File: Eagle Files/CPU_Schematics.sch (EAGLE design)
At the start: 28 parts, among them IC1 74HC574N, IC10 74HC574N, IC11 74LS541N, IC12 CY62256LL-PC, IC13 74AS04N, IC14 74AS04N, IC15 74S283N, IC16 74S283N, IC19 74ALS04N, IC2 74LS541N, IC20 74LS541N, IC3 4514N, IC4 74LS04N, IC5 74HC574N, IC6 74LS541N, IC7 CY62256LL-PC, IC8 74S283N, IC9 74S283N

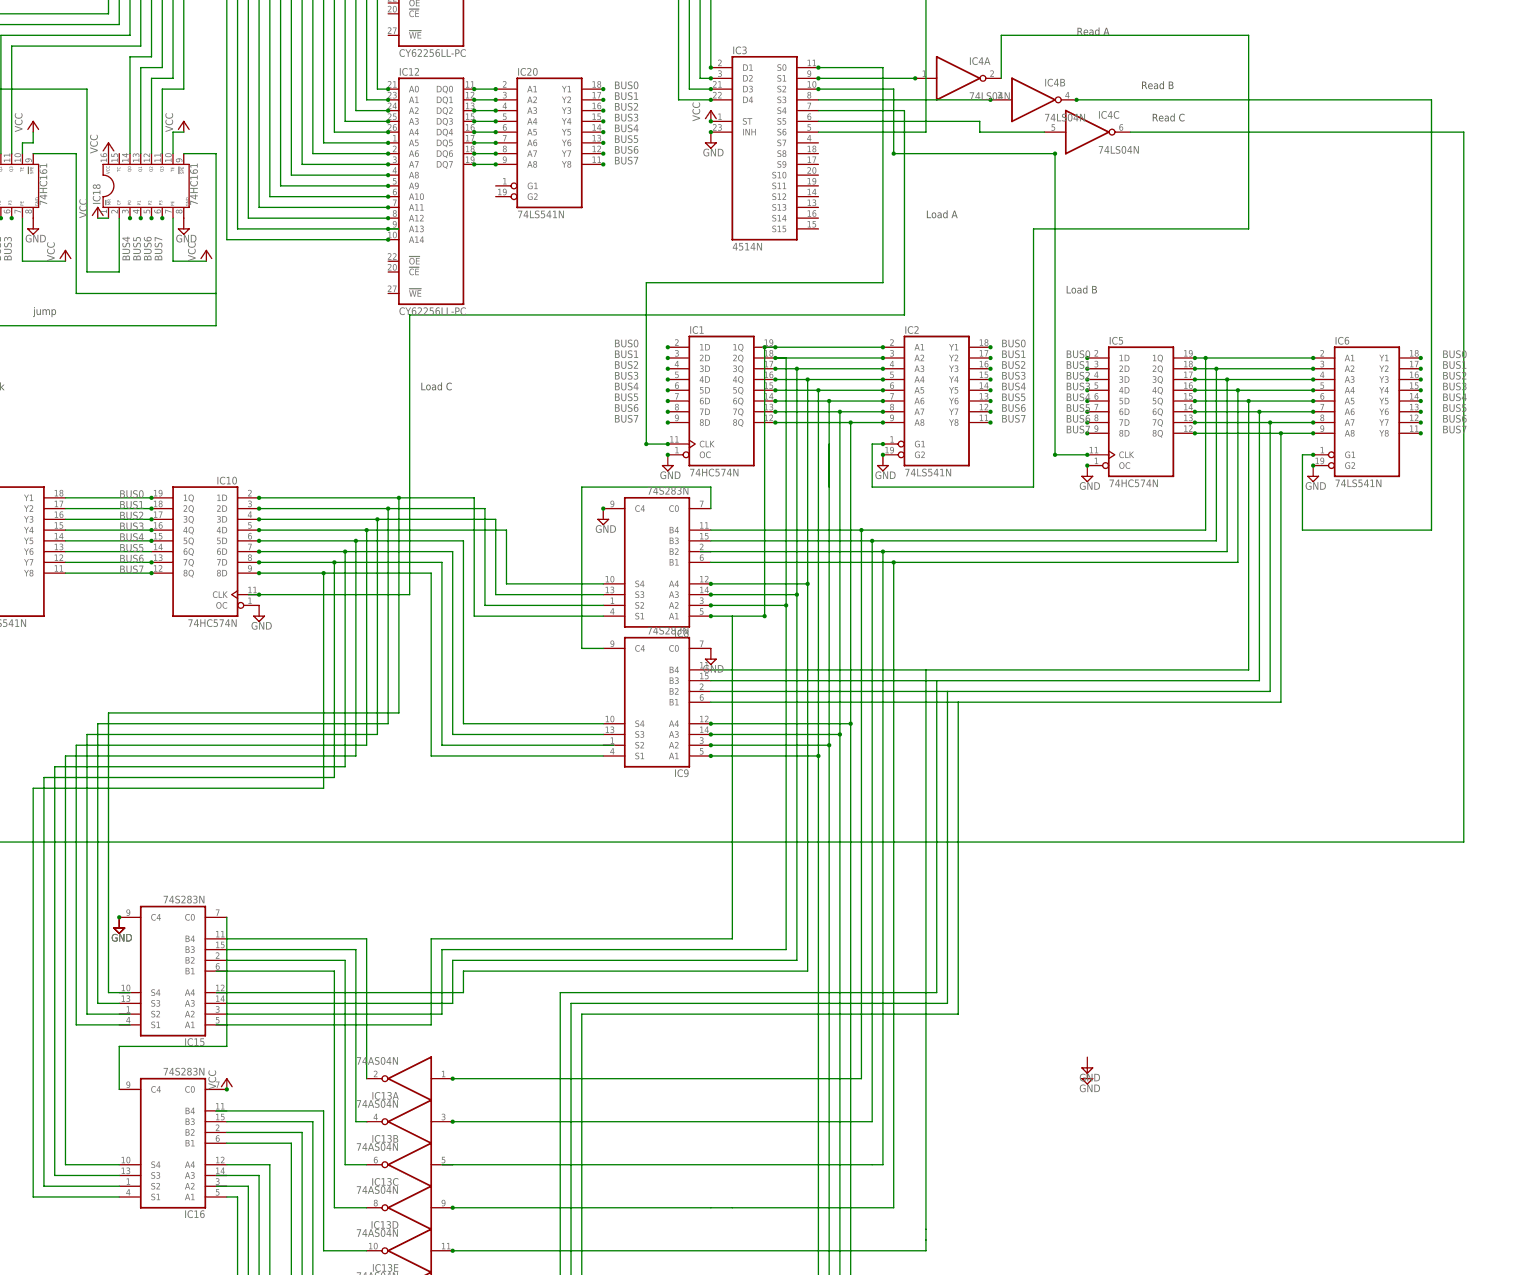
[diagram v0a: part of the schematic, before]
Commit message: Added RAM output control
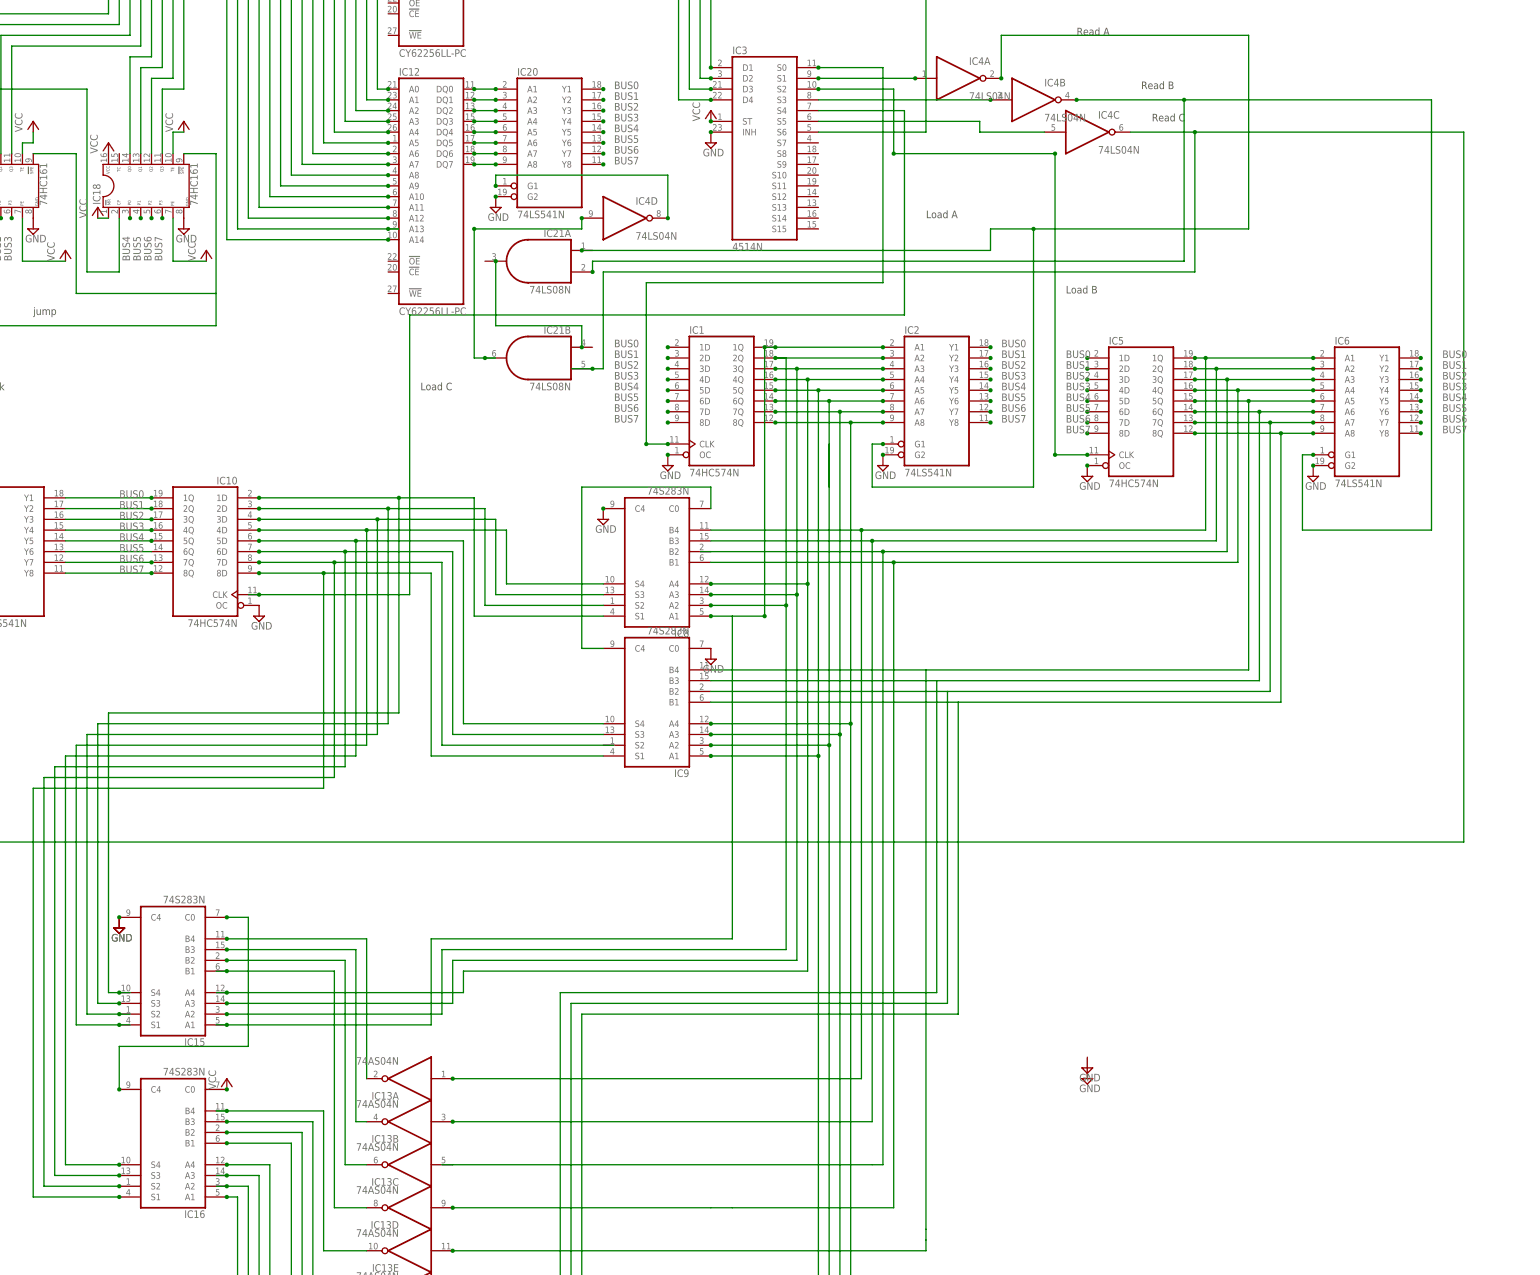
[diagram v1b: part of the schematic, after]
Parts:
- added IC21: 74LS08N, 74xx-us:74LS08N
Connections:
- new net N$75: IC21B.O, IC4D.I
- new net N$78: IC20A.G1, IC4D.O
- net GND: now also IC20A.G2
- net N$1: now also IC15A.A1
- net N$14: now also IC21A.I0
- net N$23: now also IC21A.I1
- net N$27: now also IC15A.S4
- net N$29: now also IC15A.S2
- net N$30: now also IC15A.S1
- net N$4: now also IC15A.A4
- net N$45: now also IC21B.I1
- net N$6: now also IC16A.A3
- net N$64: now also IC15A.B1
- net N$65: now also IC16A.B4
- net N$7: now also IC16A.A2
